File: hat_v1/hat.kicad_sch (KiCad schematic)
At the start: 30 parts, among them J1 GPIO, J10 Conn_01x10, J12 Speed sensor, J2 x axis motor, J3 Z axis motor, J4 x axis enc, J5 z axis enc, J6 Pot, J7 Limit switches, J8 Screw_Terminal_01x02, J9 Barrel_Jack_Switch, Q1 IRF4905, Q2 IRF4905, U3 74HC245, U4 74HC245, U6 L7805

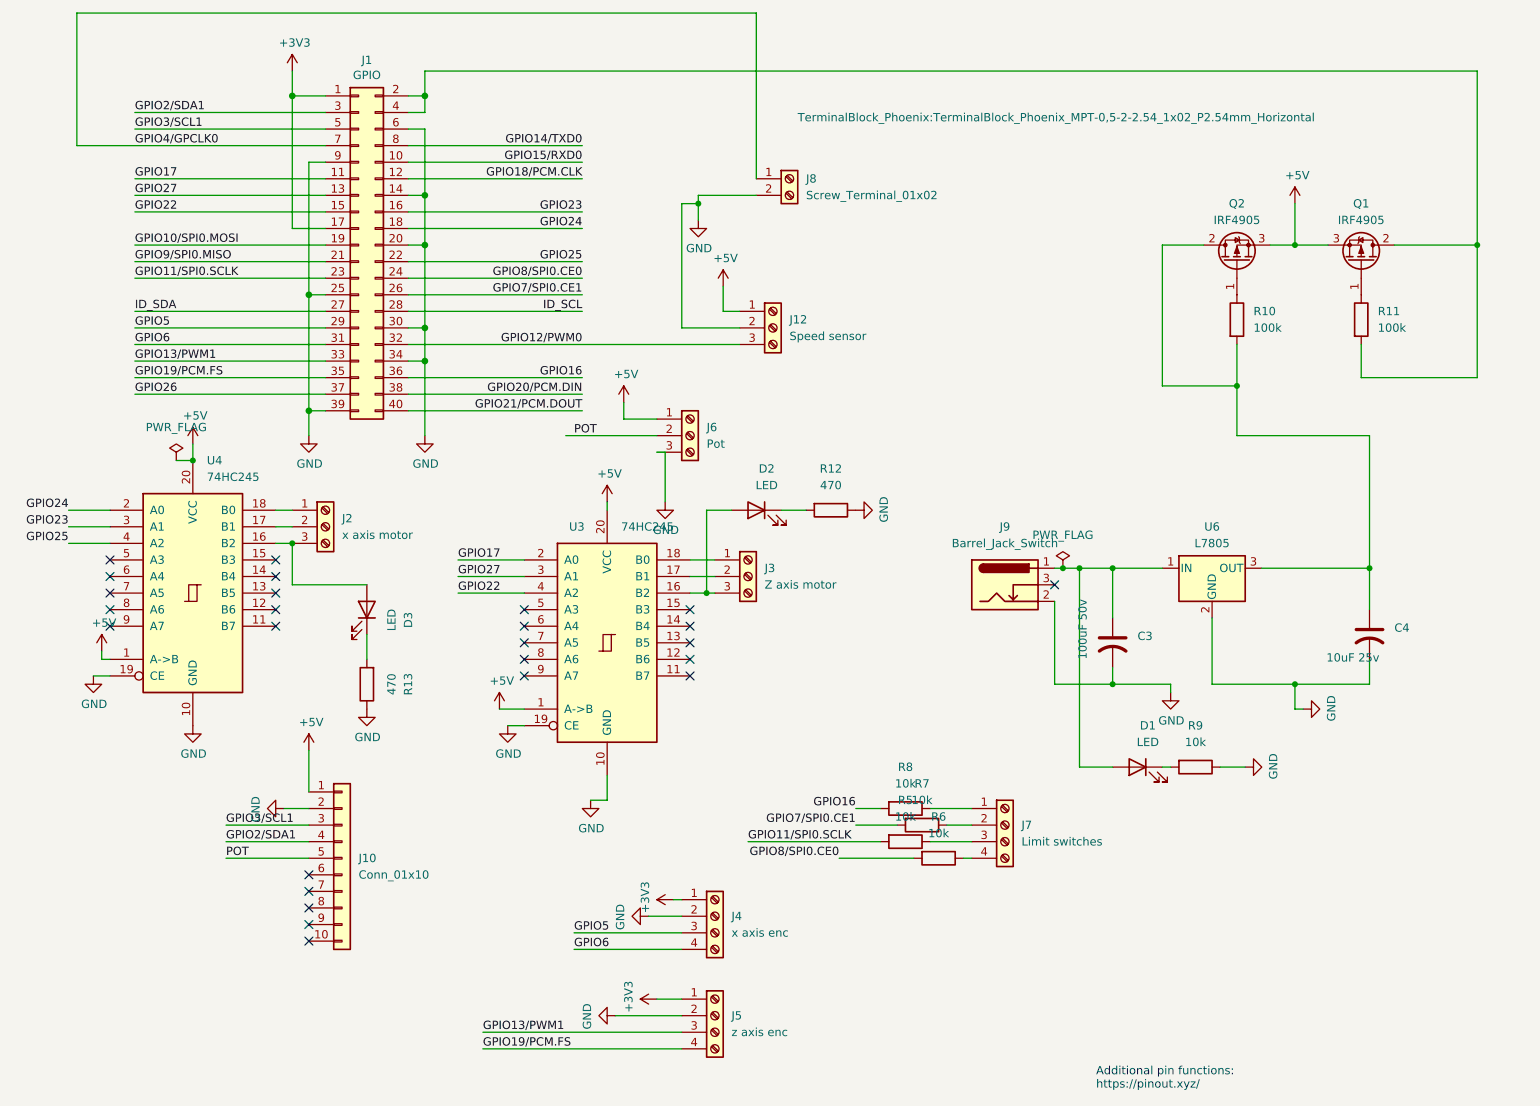
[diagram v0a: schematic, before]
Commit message: HAT design updated, rev2
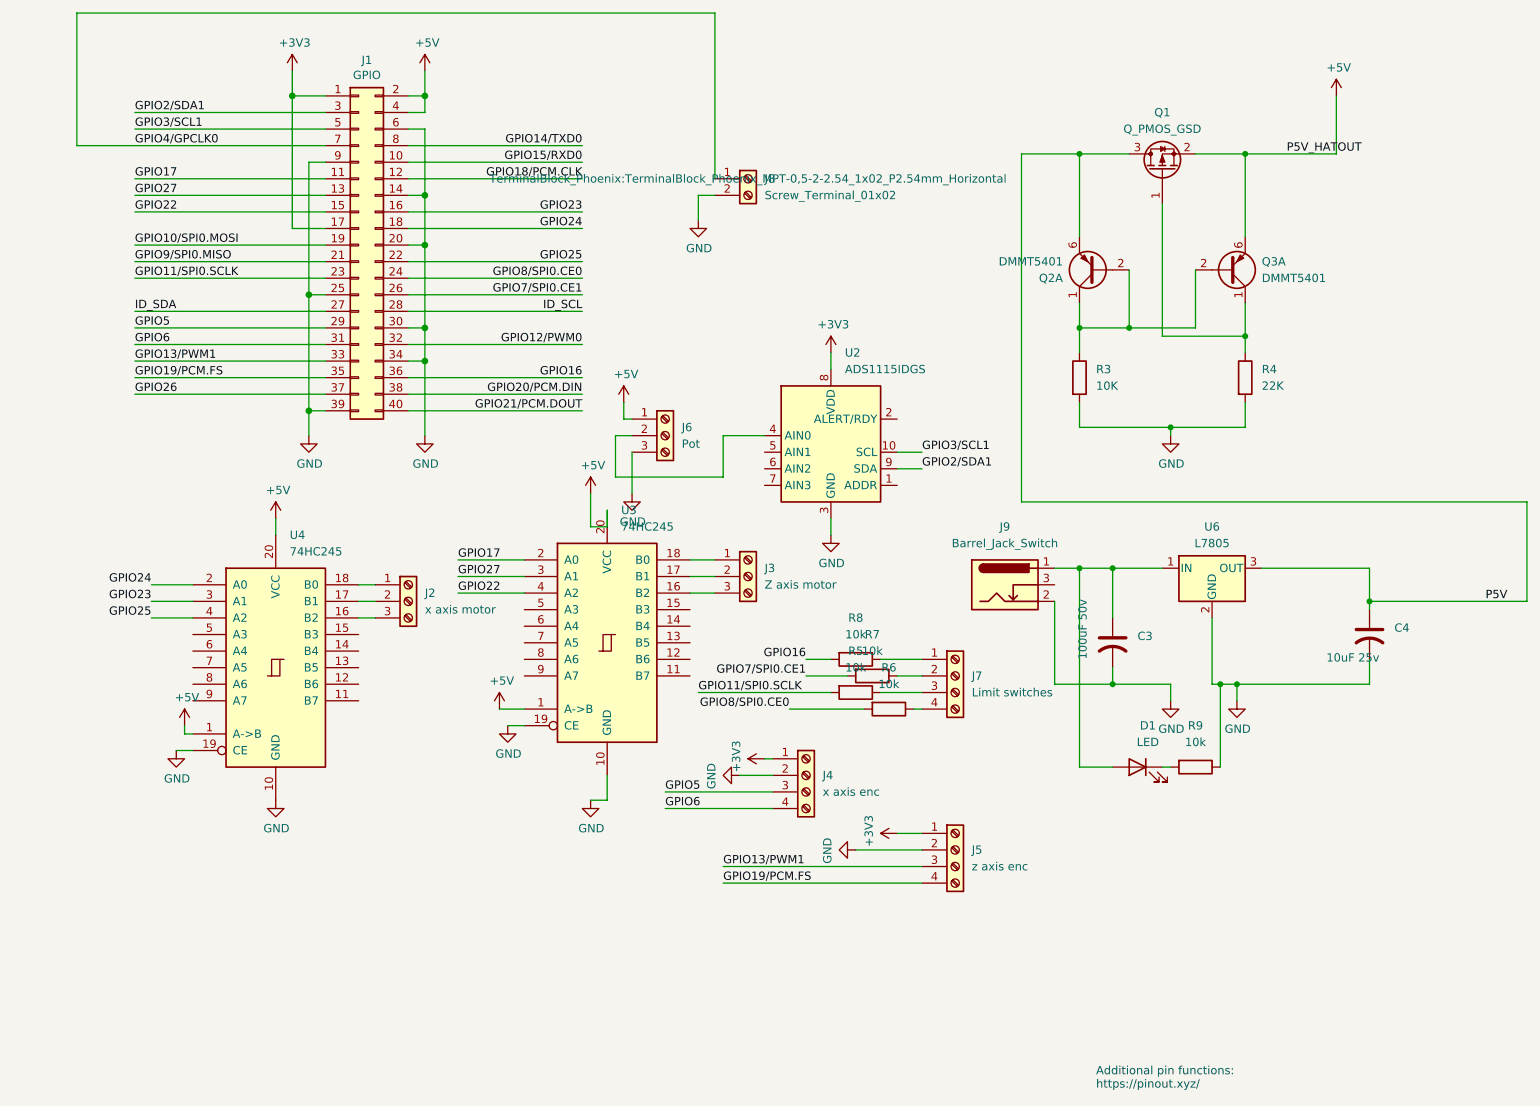
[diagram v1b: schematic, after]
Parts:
- removed D2, D3: LED, LED_THT:LED_D5.0mm, symbol Device:LED
- removed J10: Conn_01x10, Connector_PinSocket_2.54mm:PinSocket_1x10_P2.54mm_Vertical, symbol Connector_Generic:Conn_01x10
- removed J12: Speed sensor, TerminalBlock_Phoenix:TerminalBlock_Phoenix_MPT-0,5-3-2.54_1x03_P2.54mm_Horizontal, symbol Connector:Screw_Terminal_01x03
- removed Q1, Q2: IRF4905, Package_TO_SOT_THT:TO-220-3_Vertical, symbol Transistor_FET:IRF4905
- removed R10, R11: 100k, Resistor_THT:R_Axial_DIN0207_L6.3mm_D2.5mm_P7.62mm_Horizontal, symbol Device:R
- removed R12, R13: 470, Resistor_THT:R_Axial_DIN0207_L6.3mm_D2.5mm_P7.62mm_Horizontal, symbol Device:R
- added Q1: Q_PMOS_GSD, Package_TO_SOT_SMD:SOT-23, symbol Transistor_FET:Q_PMOS_GSD
- added Q2, Q3: DMMT5401, Package_TO_SOT_SMD:SOT-23-6, symbol Transistor_BJT:DMMT5401
- added R3: 10K, Resistor_THT:R_Axial_DIN0204_L3.6mm_D1.6mm_P7.62mm_Horizontal, symbol Device:R
- added R4: 22K, Resistor_THT:R_Axial_DIN0204_L3.6mm_D1.6mm_P7.62mm_Horizontal, symbol Device:R
- added U2: ADS1115IDGS, Package_SO:TSSOP-10_3x3mm_P0.5mm, symbol Analog_ADC:ADS1115IDGS
- R5, R6, R7, R8, R9: footprint Resistor_THT:R_Axial_DIN0207_L6.3mm_D2.5mm_P7.62mm_Horizontal -> Resistor_THT:R_Axial_DIN0204_L3.6mm_D1.6mm_P7.62mm_Horizontal
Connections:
- net +3V3: now also U2.8 (VDD)
- net +5V: now also J1.2 (Pin_2), J1.4 (Pin_4), Q1.2 (S), Q3.6 (E1)
- net GND: now also R3.2, R4.2, U2.3 (GND)
- net GPIO2/SDA1: now also U2.9 (SDA)
- net GPIO3/SCL1: now also U2.10 (SCL)
- net P5V: now reaches C4.1, U6.3 (OUT)
- net P5V: now also Q1.3 (D), Q2.6 (E1)
- net POT: no longer names the net of J6.2 (Pin_2)
- net POT: now also U2.4 (AIN0)
- new net: Q1.1 (G), Q3.1 (C1), R4.1
- new net: Q2.1 (C1), Q2.2 (B1), Q3.2 (B1), R3.1
- no-connect marks 26 -> 0
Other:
- moved on the sheet: J2, J4, J5, J6, J7, J8, R5, R6, R7, R8, U4
